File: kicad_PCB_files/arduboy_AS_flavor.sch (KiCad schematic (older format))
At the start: 119 parts, among them J1 SSD1306_SSH1106, J2 Expansion_port_NEW, J3 USB_B_Micro, Q1 2N7002, Q2 Si2301CDS, SW1 RST Button, SW2 UP Button, SW3 DOWN Button, SW4 LEFT Button, SW5 RIGHT Button, SW6 A Button, SW7 B Button, U1 ATmega32U4-AU, U2 W25Q128JVSIQ, U3 XC6206P33, U4 TP4054, U5 MPU-6050, Y1 16MHz

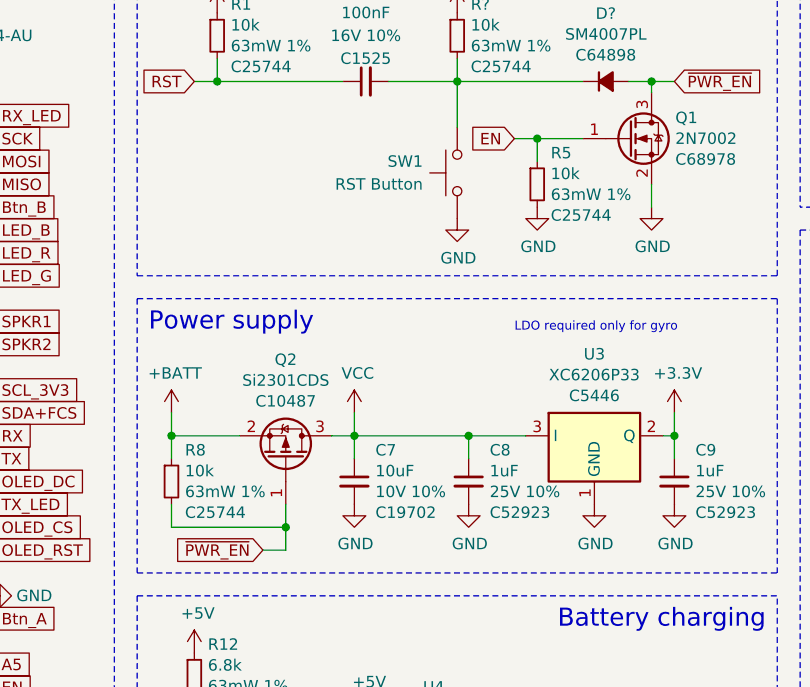
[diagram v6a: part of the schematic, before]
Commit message: Changed mosfet pullup/pulldown resistor values
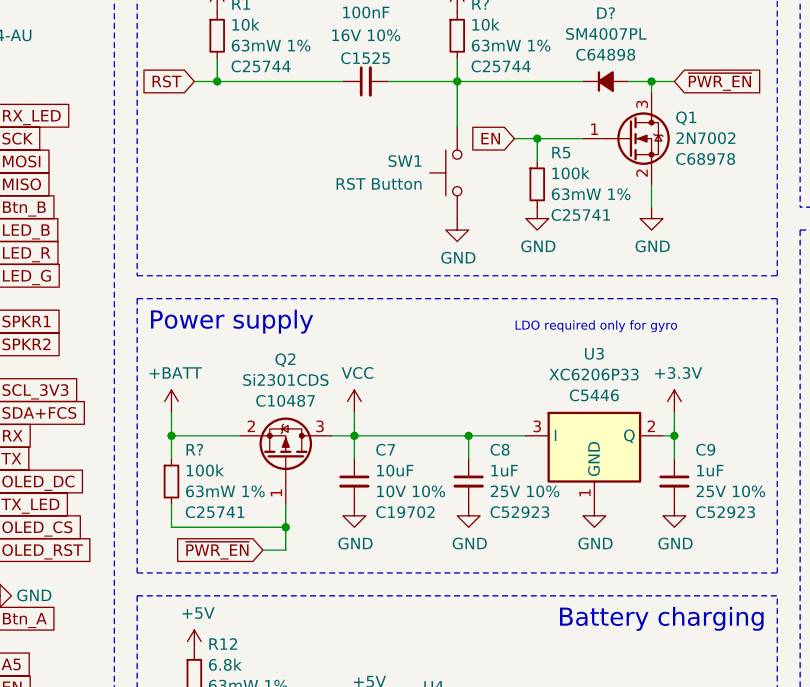
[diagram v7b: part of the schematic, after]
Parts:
- removed R8: 10k, no_refdes:0402_HandSolder, symbol Device:R_Small
- added R?: 100k, no_refdes:0402_HandSolder, symbol Device:R_Small
- R5: value 10k -> 100k; LCSC C25744 -> C25741
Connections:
- net +BATT: now also R?.1
- net ~PWR_EN: now also R?.2
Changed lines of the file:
@@
 Text GLabel 7850 4300 0    50   Input ~ 0
 SPKR2
-$Comp
-L Device:R_Small R8
-U 1 1 617AFB60
-P 2950 2850
-F 0 "R8" H 3009 2987 50  0000 L CNN
-F 1 "10k" H 3009 2896 50  0000 L CNN
-F 2 "no_refdes:0402_HandSolder" H 2950 2850 50  0001 C CNN
-F 3 "~" H 2950 2850 50  0001 C CNN
-F 4 "63mW 1%" H 3009 2805 50  0000 L CNN "Rating"
-F 5 "C25744" H 3009 2714 50  0000 L CNN "LCSC"
-	1    2950 2850
-	1    0    0    -1
-$EndComp
 Wire Wire Line
 	4750 1350 4550 1350
@@
 P 4550 1550
 F 0 "R5" H 4609 1687 50  0000 L CNN
-F 1 "10k" H 4609 1596 50  0000 L CNN
+F 1 "100k" H 4609 1596 50  0000 L CNN
 F 2 "no_refdes:0402_HandSolder" H 4550 1550 50  0001 C CNN
 F 3 "~" H 4550 1550 50  0001 C CNN
 F 4 "63mW 1%" H 4609 1505 50  0000 L CNN "Rating"
-F 5 "C25744" H 4609 1414 50  0000 L CNN "LCSC"
+F 5 "C25741" H 4609 1414 50  0000 L CNN "LCSC"
 	1    4550 1550
 	1    0    0    -1
@@
 Wire Wire Line
 	10050 3300 10050 3600
+$Comp
+L Device:R_Small R?
+U 1 1 6171FBBF
+P 2950 2850
+F 0 "R?" H 3009 2987 50  0000 L CNN
+F 1 "100k" H 3009 2896 50  0000 L CNN
+F 2 "no_refdes:0402_HandSolder" H 2950 2850 50  0001 C CNN
+F 3 "~" H 2950 2850 50  0001 C CNN
+F 4 "63mW 1%" H 3009 2805 50  0000 L CNN "Rating"
+F 5 "C25741" H 3009 2714 50  0000 L CNN "LCSC"
+	1    2950 2850
+	1    0    0    -1
+$EndComp
 $EndSCHEMATC
